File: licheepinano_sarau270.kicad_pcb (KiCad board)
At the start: 2 copper layers, 81.3 x 51.9 mm, 2 parts

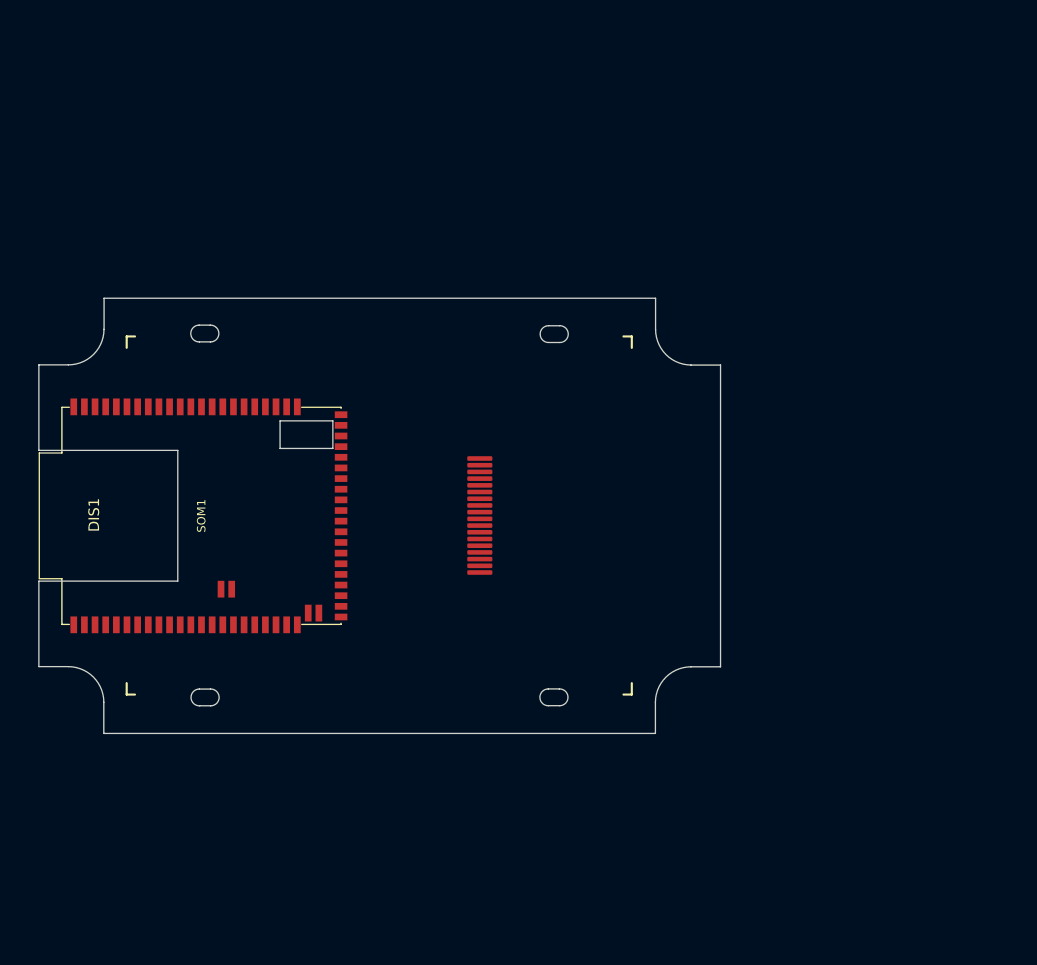
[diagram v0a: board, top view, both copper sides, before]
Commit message: Added Hub USB, Modem 3G and GPS
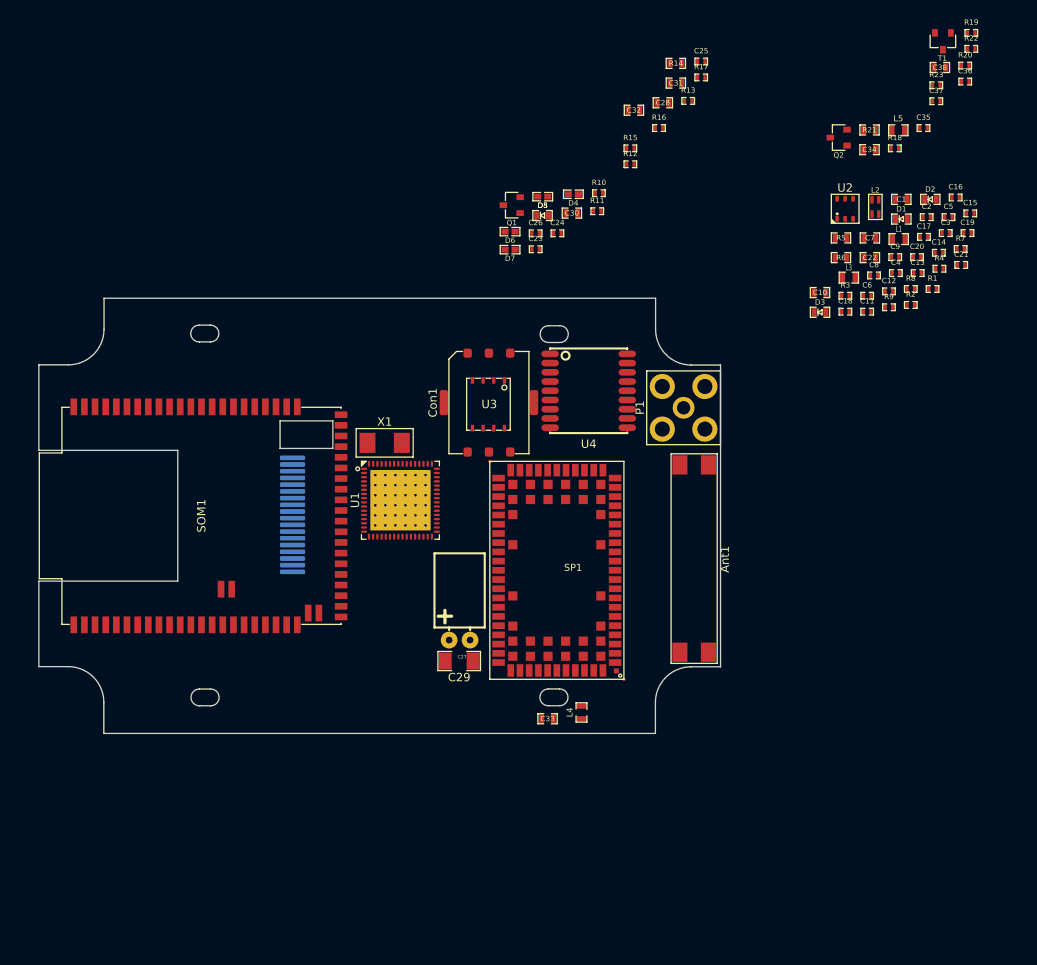
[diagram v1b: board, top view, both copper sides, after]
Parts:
- added Ant1: MEE04, Ant_Microdis:MEE04, F.Cu at (177.4, 103.5)
- added C1: 4_7uF_0603, Capacitors_Smd_0603:4_7uF_0603, F.Cu at (202.1, 60.7)
- added C10: 1uF_0603, Capacitors_Smd_0603:1uF_0603, F.Cu at (192.4, 71.8)
- added C11: 100nF_0402, Capacitors_Smd_0402:100nF_0402, F.Cu at (198.0, 74.1)
- added C12: 100nF_0402, Capacitors_Smd_0402:100nF_0402, F.Cu at (200.6, 71.6)
- added C13: 100nF_0402, Capacitors_Smd_0402:100nF_0402, F.Cu at (204.1, 69.5)
- added C14: 100nF_0402, Capacitors_Smd_0402:100nF_0402, F.Cu at (206.6, 67.0)
- added C15: 100nF_0402, Capacitors_Smd_0402:100nF_0402, F.Cu at (210.3, 62.3)
- added C16: 100nF_0402, Capacitors_Smd_0402:100nF_0402, F.Cu at (208.6, 60.4)
- added C17: 100nF_0402, Capacitors_Smd_0402:100nF_0402, F.Cu at (204.8, 65.1)
- added C18: 100nF_0402, Capacitors_Smd_0402:100nF_0402, F.Cu at (195.4, 74.1)
- added C19: 100nF_0402, Capacitors_Smd_0402:100nF_0402, F.Cu at (210.0, 64.7)
- added C2: 100nF_0402, Capacitors_Smd_0402:100nF_0402, F.Cu at (205.1, 62.8)
- added C20: 100nF_0402, Capacitors_Smd_0402:100nF_0402, F.Cu at (204.0, 67.6)
- added C21: 100nF_0402, Capacitors_Smd_0402:100nF_0402, F.Cu at (209.3, 68.5)
- added C22: 100nF_0603, Capacitors_Smd_0603:100nF_0603, F.Cu at (198.4, 67.6)
- added C23: 47pF_0402, Capacitors_Smd_0402:47pF_0402, F.Cu at (158.5, 66.6)
- added C24: 47pF_0402, Capacitors_Smd_0402:47pF_0402, F.Cu at (161.1, 64.7)
- added C25: 47pF_0402, Capacitors_Smd_0402:47pF_0402, F.Cu at (178.2, 44.2)
- added C26: 47pF_0402, Capacitors_Smd_0402:47pF_0402, F.Cu at (158.5, 64.7)
- added C27: 220uF_6_3V_Polymer, Discrete_Electrolytic:220uF_6_3V_Polymer_Horizontal_fi8_len8mm, F.Cu at (149.4, 113.2)
- added C28: 100nF_0603, Capacitors_Smd_0603:100nF_0603, F.Cu at (173.7, 49.1)
- added C29: 47uF_1206, Capacitors_Smd_1206:47uF_1206, F.Cu at (149.4, 115.7)
- added C3: 30pF_0402, Capacitors_Smd_0402:30pF_0402, F.Cu at (207.4, 64.7)
- added C30: 100nF_0603, Capacitors_Smd_0603:100nF_0603, F.Cu at (162.8, 62.3)
- added C31: 100nF_0603, Capacitors_Smd_0603:100nF_0603, F.Cu at (175.2, 46.8)
- added C32: 100nF_0603, Capacitors_Smd_0603:100nF_0603, F.Cu at (170.2, 50.0)
- added C33: 10pF_0603, Capacitors_Smd_0603:10pF_0603, F.Cu at (159.9, 122.6)
- added C34: 1uF_0603, Capacitors_Smd_0603:1uF_0603, F.Cu at (198.3, 54.7)
- added C35: 100nF_0402, Capacitors_Smd_0402:100nF_0402, F.Cu at (204.8, 52.2)
- added C36: 100nF_0402, Capacitors_Smd_0402:100nF_0402, F.Cu at (209.7, 46.6)
- added C37: 100nF_0402, Capacitors_Smd_0402:100nF_0402, F.Cu at (206.3, 49.0)
- added C38: 1uF_0603, Capacitors_Smd_0603:1uF_0603, F.Cu at (206.7, 44.9)
- added C4: 30pF_0402, Capacitors_Smd_0402:30pF_0402, F.Cu at (201.5, 69.5)
- added C5: 100nF_0402, Capacitors_Smd_0402:100nF_0402, F.Cu at (207.7, 62.8)
- added C6: 100nF_0402, Capacitors_Smd_0402:100nF_0402, F.Cu at (198.0, 72.2)
- added C7: 4_7uF_0603, Capacitors_Smd_0603:4_7uF_0603, F.Cu at (198.4, 65.3)
- added C8: 100nF_0402, Capacitors_Smd_0402:100nF_0402, F.Cu at (198.9, 69.7)
- added C9: 100nF_0402, Capacitors_Smd_0402:100nF_0402, F.Cu at (201.4, 67.6)
- added Con1: SIM8050-6-0-14-01-A, SimCard_Holders:SIM8050-6-0-14-01-A, F.Cu at (152.9, 84.9)
- added D1: KPG-1608SURKC-T, Diodes:LED_KPG-1608SURKC-T, F.Cu at (202.1, 63.0)
- added D2: KPT-1608CGCK, Diodes:LED_KPT-1608CGCK, F.Cu at (205.6, 60.7)
- added D3: KP-1608YC, Diodes:LED_KP-1608YC, F.Cu at (192.4, 74.1)
- added D4: PESD0402-140, Diodes:PESD0402-140, F.Cu at (163.0, 60.0)
- added D5: PESD0402-140, Diodes:PESD0402-140, F.Cu at (159.3, 60.3)
- added D6: PESD0402-140, Diodes:PESD0402-140, F.Cu at (155.4, 64.5)
- added D7: PESD0402-140, Diodes:PESD0402-140, F.Cu at (155.4, 66.7)
- added D8: KPG-1608SURKC-T, Diodes:LED_KPG-1608SURKC-T, F.Cu at (159.3, 62.6)
- added L1: LCBA-601, Inductors:LCBA-601, F.Cu at (201.8, 65.4)
- added L2: DLW21HN900SQ2L, Inductors:DLW21HN900SQ2L, F.Cu at (199.0, 61.6)
- added L3: LCBA-601, Inductors:LCBA-601, F.Cu at (195.9, 70.0)
- added L4: 39nH_0603, Inductors:39nH_0603, F.Cu at (164.0, 121.9)
- added L5: 39nH_0603, Inductors:39nH_0603, F.Cu at (201.8, 52.4)
- added P1: RF2-03E-T-00-50-G, RF_Connectors:RF2-03E-T-00-50-G, F.Cu at (176.1, 85.5)
- added Q1: BC847B, Transistor_Bipolar:BC847B_SOT23, F.Cu at (155.6, 61.3)
- added Q2: BC847B, Transistor_Bipolar:BC847B_SOT23, F.Cu at (194.6, 53.3)
- added R1: 12k4_0402_1%, Resistor_Smd_0402:12k4_0402, F.Cu at (205.8, 71.4)
- added R10: 10k_0402, Resistor_Smd_0402:10k_0402, F.Cu at (166.0, 59.9)
- added R11: 10k_0402, Resistor_Smd_0402:10k_0402, F.Cu at (165.8, 62.1)
- added R12: 10k_0402, Resistor_Smd_0402:10k_0402, F.Cu at (169.8, 56.5)
- added R13: 100k_0402, Resistor_Smd_0402:100k_0402, F.Cu at (176.7, 48.9)
- added R14: 0R_0603, Resistor_Smd_0603:0R_0603, F.Cu at (175.2, 44.4)
- added R15: 10k_0402, Resistor_Smd_0402:10k_0402, F.Cu at (169.8, 54.6)
- added R16: 47k_0402, Resistor_Smd_0402:47k_0402, F.Cu at (173.2, 52.2)
- added R17: 470R_0402, Resistor_Smd_0402:470R_0402, F.Cu at (178.2, 46.1)
- added R18: 100k_0402, Resistor_Smd_0402:100k_0402, F.Cu at (201.3, 54.6)
- added R19: 10k_0402, Resistor_Smd_0402:10k_0402, F.Cu at (210.5, 40.8)
- added R2: 10k_0402, Resistor_Smd_0402:10k_0402, F.Cu at (203.2, 73.3)
- added R20: 47k_0402, Resistor_Smd_0402:47k_0402, F.Cu at (209.7, 44.7)
- added R21: 10R_0603_1%, Resistor_Smd_0603:10R_0603, F.Cu at (198.3, 52.4)
- added R22: 2k7_0402, Resistor_Smd_0402:2k7_0402, F.Cu at (210.5, 42.7)
- added R23: 2k7_0402, Resistor_Smd_0402:2k7_0402, F.Cu at (206.3, 47.1)
- added R3: 1M_0402, Resistor_Smd_0402:1M_0402, F.Cu at (195.4, 72.2)
- added R4: 12k_0402_1%, Resistor_Smd_0402:12k_0402, F.Cu at (206.7, 68.9)
- added R5: 0R_0603, Resistor_Smd_0603:0R_0603, F.Cu at (194.9, 65.3)
- added R6: 0R_0603, Resistor_Smd_0603:0R_0603, F.Cu at (194.9, 67.6)
- added R7: 470R_0402, Resistor_Smd_0402:470R_0402, F.Cu at (209.2, 66.6)
- added R8: 470R_0402, Resistor_Smd_0402:470R_0402, F.Cu at (203.2, 71.4)
- added R9: 470R_0402, Resistor_Smd_0402:470R_0402, F.Cu at (200.6, 73.5)
- added SP1: Sara_U270, UBlox:Sara_U270, F.Cu at (161.0, 104.9)
- added T1: FDN304P, Transistor_Mosfet:FDN304P_SOT23, F.Cu at (207.1, 41.8)
- added U1: LAN9514I, Communication_Interfaces:LAN9514I, F.Cu at (142.4, 96.5)
- added U2: IP4220CZ6, ESD_Protectors:IP4220CZ6_SOT457, F.Cu at (195.4, 61.8)
- added U3: Full_M2M_Quad_SIM DNF, SIMchip:Full_M2M_Quad_SIM, F.Cu at (152.9, 85.1)
- added U4: MAX-M8C, UBlox_GPS:Max-M8C, F.Cu at (164.8, 83.5)
- added X1: ABM3-25.000MHZ-D2Y-T, Resonators:ABM3-25.000MHZ-D2Y-T, F.Cu at (140.5, 89.7)
- DIS1: moved to B.Cu
- moved DIS1 1.66 mm to (141.5, 98.3)

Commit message: Added logic level shifter on pcb
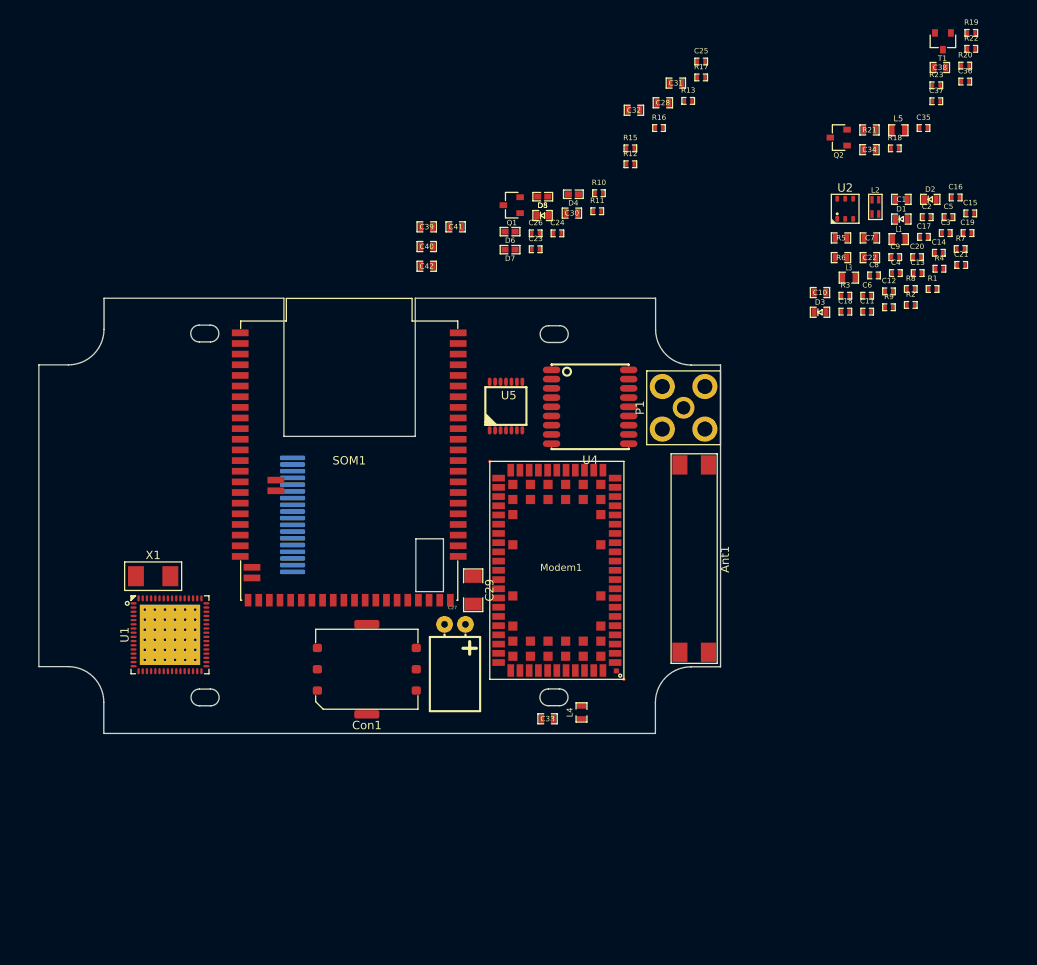
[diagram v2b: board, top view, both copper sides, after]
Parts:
- removed R14: 0R_0603, Resistor_Smd_0603:0R_0603
- removed U3: Full_M2M_Quad_SIM DNF, SIMchip:Full_M2M_Quad_SIM
- added C39: 1uF/6V3, Capacitors_Smd_0603:1uF_0603, F.Cu at (145.5, 63.9)
- added C40: 100nF/50V, Capacitors_Smd_0603:100nF_0603, F.Cu at (145.5, 66.3)
- added C41: 1uF/6V3, Capacitors_Smd_0603:1uF_0603, F.Cu at (148.9, 63.9)
- added C42: 100nF/50V, Capacitors_Smd_0603:100nF_0603, F.Cu at (145.5, 68.6)
- added U5: TXB0104, Logic_Voltage_Shifter:TXB0104_TSSOP14, F.Cu at (154.9, 85.3)
- C1, C7: value 4_7uF_0603 -> 4.7uF/6V3
- C10, C34, C38: value 1uF_0603 -> 1uF/6V3
- C11, C12, C13, C14, C15, C16, C17, C18, C19, C2, C20, C21, C35, C36, C37, C5, C6, C8, C9: value 100nF_0402 -> 100nF/50V
- C22, C28, C30, C31, C32: value 100nF_0603 -> 100nF/50V
- C23, C24, C25, C26: value 47pF_0402 -> 47pF/50V
- C27: value 220uF_6_3V_Polymer -> 220uF/6V3
- C29: value 47uF_1206 -> 47uF/6V3
- C3, C4: value 30pF_0402 -> 30pF/50V
- C33: value 10pF_0603 -> 10pF
- L4, L5: value 39nH_0603 -> 39nH
- R1: value 12k4_0402_1% -> 12k/1%
- R10, R11, R12, R15, R19, R2: value 10k_0402 -> 10k
- R13, R18: value 100k_0402 -> 100k
- R16, R20: value 47k_0402 -> 47k
- R17, R7, R8, R9: value 470R_0402 -> 470R
- R21: value 10R_0603_1% -> 10R/1%
- R22, R23: value 2k7_0402 -> 2k7
- R3: value 1M_0402 -> 1M
- R4: value 12k_0402_1% -> 12k/1%
- R5, R6: value 0R_0603 -> 0R
- moved Con1 35.0 mm to (138.3, 116.7), turned to 180 degrees
- moved X1 31.9 mm to (112.9, 105.6)
- moved U1 31.8 mm to (114.9, 112.6)
- moved SOM1 18.8 mm to (136.2, 91.8), turned to 180 degrees
- moved C29 8.60 mm to (151.0, 107.3), turned to 90 degrees
- moved C27 1.95 mm to (148.9, 111.4), turned to 180 degrees
- moved U4 1.92 mm to (165.0, 85.4)
- renumbered SP1 to Modem1
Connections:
- net /Modem 3G/LOCAL_MODEM_~W_DISABLE renamed /Modem 3G/MODEM_PWR_ON
- net /Modem 3G/MPCIE_SIM_CLK renamed /Modem 3G/SIM_CLK
- net /Modem 3G/MPCIE_SIM_DET renamed /Modem 3G/SIM_DET
- net /Modem 3G/MPCIE_SIM_IO renamed /Modem 3G/SIM_IO
- net /Modem 3G/MPCIE_SIM_RST renamed /Modem 3G/SIM_RST
- net /Modem 3G/MPCIE_VSIM renamed /Modem 3G/VSIM
- net /USB Hub Module/USB_EXTERNAL_D+ renamed /USB Hub Module/USB_D2_OUT_P
- net /USB Hub Module/USB_EXTERNAL_D- renamed /USB Hub Module/USB_D2_OUT_N
- net 3V3 renamed /USB Hub Module/POWER_IN_3V3
- net 3V8 renamed /Modem 3G/MODEM_POWER_IN
- C37 pad 1: +1.8V -> /GPS Module/1V8
- DIS1 pad 1: (no net) -> /LCD Module/POWER_IN_GND
- DIS1 pad 8: (no net) -> /LCD Module/POWER_IN_GND
- Modem1 pad 4: Net-(R14-Pad2) -> /Modem 3G/POWER_OUT_1V8
- R10 pad 2: +1.8V -> /Modem 3G/POWER_OUT_1V8
- R18 pad 2: +1.8V -> /GPS Module/POWER_IN_1V8
- R22 pad 2: +1.8V -> /GPS Module/1V8
- R23 pad 2: +1.8V -> /GPS Module/1V8
- T1 pad S: +1.8V -> /GPS Module/POWER_IN_1V8
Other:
- outline, holes or cut-outs redrawn

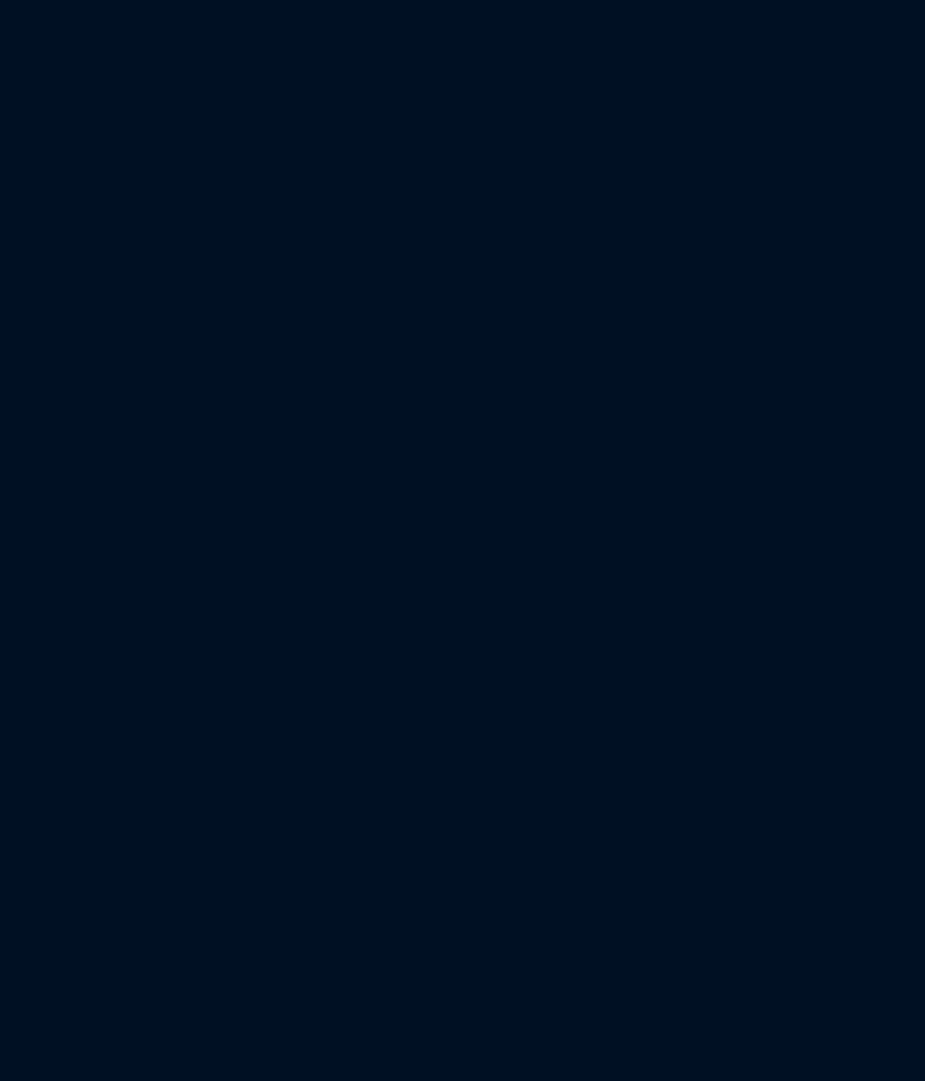
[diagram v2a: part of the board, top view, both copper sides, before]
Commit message: Added ethernet connector on pcb
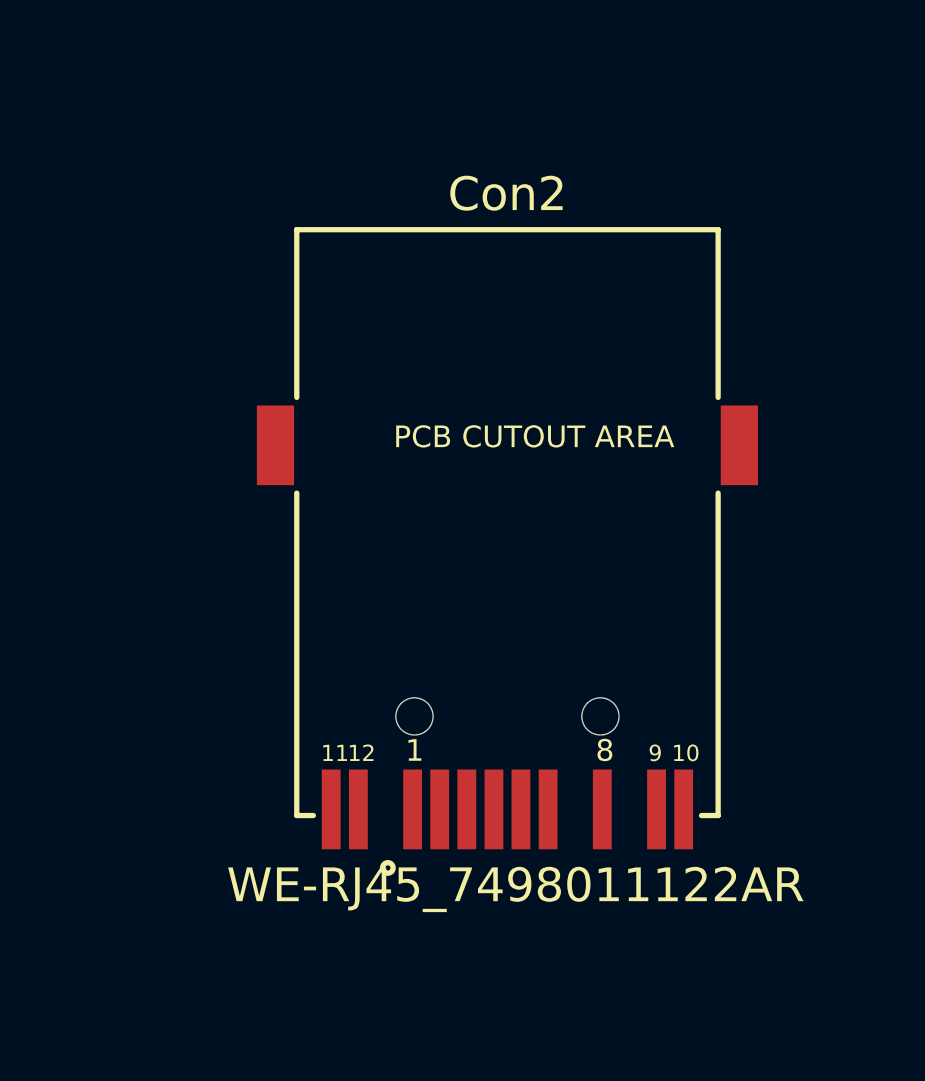
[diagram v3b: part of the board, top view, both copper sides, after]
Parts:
- added Con2: WE-RJ45_7498011122AR, RJ45_Ethernet_Transformer:WE-RJ45_7498011122AR, F.Cu at (201.3, 108.3)
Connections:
- Modem1 pad 12: (no net) -> /Logic Voltage Shifter/SIG3_LOW_PART
- Modem1 pad 13: (no net) -> /Logic Voltage Shifter/SIG4_LOW_PART
- Modem1 pad 23: (no net) -> /GPS Module/GNSS_ENABLE
- Modem1 pad 24: (no net) -> /Logic Voltage Shifter/SIG2_LOW_PART
- Modem1 pad 25: (no net) -> /GPS Module/GPS_EXTINT
- Modem1 pad 26: (no net) -> /Modem 3G/GPS_I2C_1V8_SDA
- Modem1 pad 27: (no net) -> /Modem 3G/GPS_I2C_1V8_SCL
- Modem1 pad 28: (no net) -> /USB Hub Module/USB_D2_OUT_N
- Modem1 pad 29: (no net) -> /USB Hub Module/USB_D2_OUT_P
- Modem1 pad 4: /Modem 3G/POWER_OUT_1V8 -> /GPS Module/POWER_IN_1V8
- R10 pad 2: /Modem 3G/POWER_OUT_1V8 -> /GPS Module/POWER_IN_1V8
- R19 pad 2: (no net) -> /GPS Module/GNSS_ENABLE
- R22 pad 1: /GPS Module/I2C_1V8_SCL -> /Modem 3G/GPS_I2C_1V8_SCL
- R23 pad 1: /GPS Module/I2C_1V8_SDA -> /Modem 3G/GPS_I2C_1V8_SDA
- U4 pad 16: /GPS Module/I2C_1V8_SDA -> /Modem 3G/GPS_I2C_1V8_SDA
- U4 pad 17: /GPS Module/I2C_1V8_SCL -> /Modem 3G/GPS_I2C_1V8_SCL
- U4 pad 2: (no net) -> /Logic Voltage Shifter/SIG2_LOW_PART
- U4 pad 3: (no net) -> /Logic Voltage Shifter/SIG1_LOW_PART
- U4 pad 5: (no net) -> /GPS Module/GPS_EXTINT
- U5 pad 10: (no net) -> /Logic Voltage Shifter/SIG4_LOW_PART
- U5 pad 11: (no net) -> /Logic Voltage Shifter/SIG3_LOW_PART
- U5 pad 12: (no net) -> /Logic Voltage Shifter/SIG2_LOW_PART
- U5 pad 13: (no net) -> /Logic Voltage Shifter/SIG1_LOW_PART
